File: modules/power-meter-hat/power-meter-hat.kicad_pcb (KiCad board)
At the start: 2 copper layers, 65 x 56 mm, 48 parts, among them J1 GPIO, J2 Barrel_Jack_Switch, J3 Conn_01x02, J4 Conn_01x02, J5 Conn_01x02, U1 CAT24C256, U2 NCP1117-3.3_SOT223, U3 INA219AxD, U4 INA219AxD, U5 INA219AxD

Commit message: Update components and footprints
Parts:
- C1: value 100n -> C_Small
- C2, C3: value 22u -> C
- D1, D2, D3, D4, D5: footprint LED_SMD:LED_1206_3216Metric_Castellated -> LED_SMD:LED_1206_3216Metric
- J1: value GPIO -> Conn_02x20_Odd_Even
- JP1: value ID_WP -> SolderJumper_2_Open
- JP10, JP11, JP3, JP4, JP5, JP6, JP7, JP8, JP9: value Jumper_NC_Dual -> Jumper_3_Open
- JP2: value Jumper -> SolderJumper_2_Open
- R1, R2: value 3.9k -> R_Small
- R10, R12, R3, R4, R8: value 220R -> R
- R11, R7, R9: value ? -> R
- R5, R6: value 10k -> R
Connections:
- net +3V3 renamed +3.3V

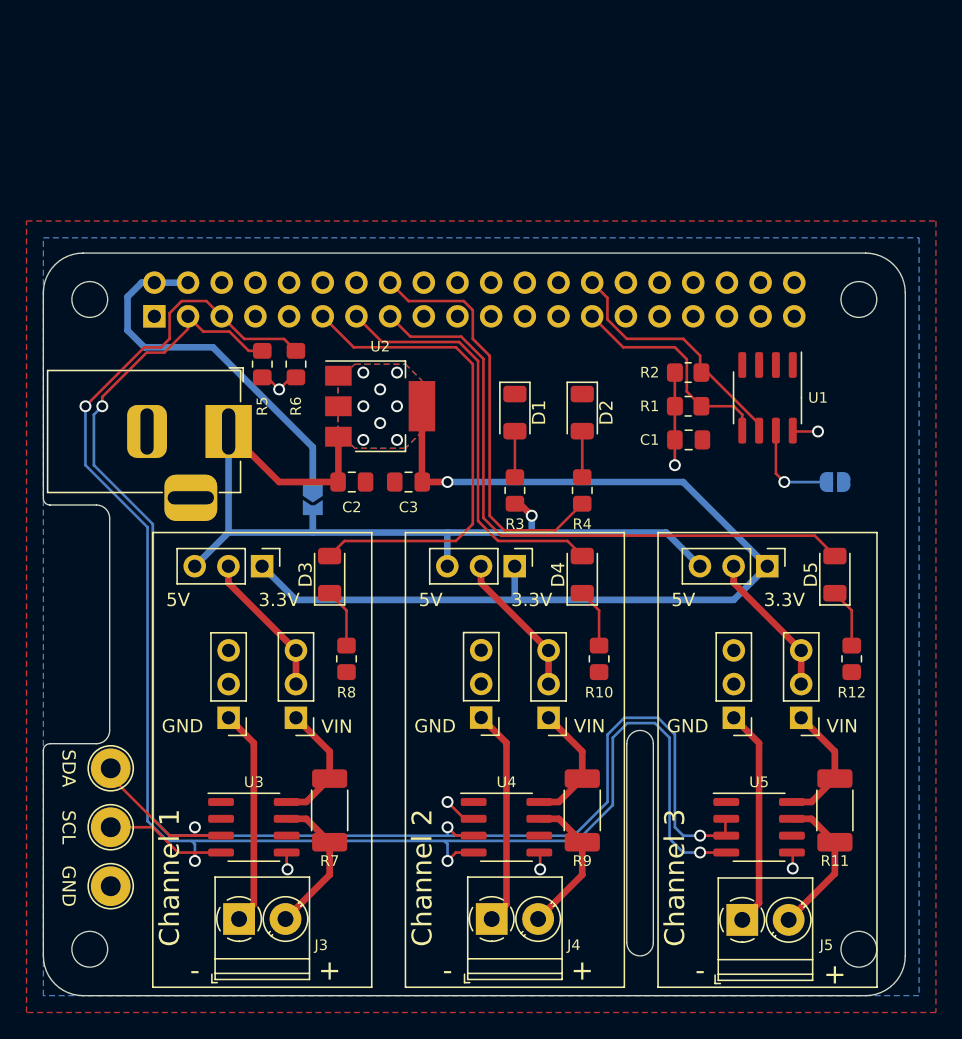
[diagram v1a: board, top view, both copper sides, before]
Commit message: Add "ideal diode" and fuse, update values
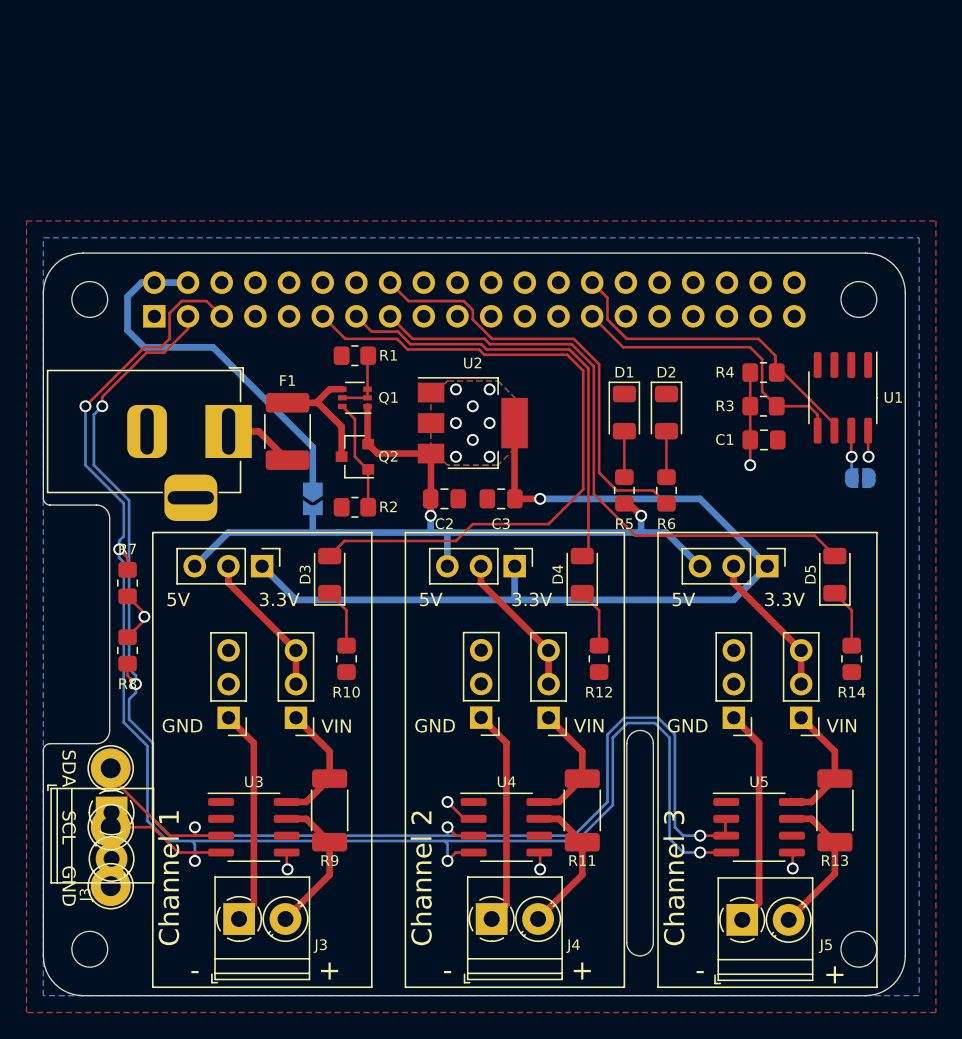
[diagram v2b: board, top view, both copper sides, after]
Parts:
- added F1: MF-MSMF250/16X-2, Fuse:Fuse_1812_4532Metric_Castellated, F.Cu at (118.4, 57.5)
- added J3: OutputTerminal, TerminalBlock_Phoenix:TerminalBlock_Phoenix_PT-1,5-2-3.5-H_1x02_P3.50mm_Horizontal, F.Cu at (105.1, 86.2)
- added Q1: BC856BDW1, Package_TO_SOT_SMD:SOT-363_SC-70-6, F.Cu at (123.5, 54.9)
- added Q2: SI2301CDS, Package_TO_SOT_SMD:SOT-23, F.Cu at (123.5, 59.4)
- added R1: 10k, Resistor_SMD:R_0805_2012Metric_Pad1.20x1.40mm_HandSolder, F.Cu at (123.5, 51.7)
- added R2: 47k, Resistor_SMD:R_0805_2012Metric_Pad1.20x1.40mm_HandSolder, F.Cu at (123.5, 63.2)
- C1: value C_Small -> 100n
- C2, C3: value C -> 22u
- J2: renamed from J1; value Conn_02x20_Odd_Even -> GPIO
- J3, J4, J5: value Conn_01x02 -> OutputTerminal
- JP1: value SolderJumper_2_Open -> ID_WP
- JP10, JP11, JP3, JP4, JP5, JP6, JP7, JP8, JP9: value Jumper_3_Open -> Jumper
- JP2: value SolderJumper_2_Open -> 5V_Bridge
- R10: renamed from R8; value R -> 220R
- R12: renamed from R10; value R -> 220R
- R14: renamed from R12; value R -> 220R
- R3: renamed from R1; value R_Small -> 3.9k
- R4: renamed from R2; value R_Small -> 3.9k
- R5: renamed from R3; value R -> 220R
- R6: renamed from R4; value R -> 220R
- R7: renamed from R5; value R -> 10k
- R8: renamed from R6; value R -> 10k
- moved R7 23.9 mm to (106.3, 74.0), turned to -90 degrees
- moved R8 20.8 mm to (106.3, 68.9)
- moved D1 8.25 mm to (143.8, 56.0)
- moved R5 8.25 mm to (143.8, 61.9)
- moved C3 7.10 mm to (134.5, 62.5)
- moved C2 7.10 mm to (130.2, 62.5)
- moved U2 7.10 mm to (132.4, 56.8)
- moved D2 6.35 mm to (147.0, 56.0)
- moved R6 6.35 mm to (147.0, 61.9)
- moved C1 5.68 mm to (154.3, 58.1)
- moved R3 5.68 mm to (154.3, 55.5)
- moved R4 5.68 mm to (154.3, 53.0)
- moved U1 5.68 mm to (160.3, 54.9)
- moved JP1 1.93 mm to (161.6, 61.0)
- renumbered J2 to J1, R9 to R11, R11 to R13, R7 to R9
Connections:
- J1 pad 1: +5VP -> /Vpsu
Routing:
- net /GPIO[17]: track 36.7 -> 51.5 mm
- net /Vfused: track 0.00 -> 9.44 mm
- net Net-(Q1-Pad6): track 0.00 -> 8.44 mm
- net +3.3VP: track 77.1 -> 69.6 mm
- net +5VP: track 68.4 -> 61.3 mm, vias 1 -> 2
- net /ID_SCL: track 19.2 -> 24.9 mm
- net /ID_SDA: track 17.0 -> 22.7 mm
- net /Vpsu: track 0.00 -> 5.34 mm
- net Net-(Q1-Pad2): track 0.00 -> 5.10 mm
- net /SCL: track 129.7 -> 125.1 mm, vias 4 -> 5
- net /SDA: track 124.5 -> 120.1 mm, vias 4 -> 5
- net Net-(JP1-Pad1): track 7.31 -> 3.59 mm
- net /GPIO[27]: track 31.6 -> 33.5 mm
- net /GPIO[23]: track 31.4 -> 33.0 mm
- net /GPIO[22]: track 48.0 -> 46.7 mm
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
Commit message: Fix PCB
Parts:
- removed the J3 at (105.1, 86.2)
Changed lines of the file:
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@@
-  )
-  (footprint "TerminalBlock_Phoenix:TerminalBlock_Phoenix_PT-1,5-2-3.5-H_1x02_P3.50mm_Horizontal" (layer "F.Cu")
-    (at 105.145 86.185 -90)
-    (descr "Terminal Block Phoenix PT-1,5-2-3.5-H, 2 pins, pitch 3.5mm, size 7x7.6mm^2, drill diamater 1.2mm, pad diameter 2.4mm, see , script-generated using https://github.com/pointhi/kicad-footprint-generator/scripts/TerminalBlock_Phoenix")
-    (tags "THT Terminal Block Phoenix PT-1,5-2-3.5-H pitch 3.5mm size 7x7.6mm^2 drill 1.2mm pad 2.4mm")
-    (property "Sheetfile" "power_channel.kicad_sch")
-    (property "Sheetname" "PowerChannel 1")
-    (attr through_hole)
-    (fp_text reference "J3" (at 6.195 1.97 90) (layer "F.SilkS")
-      (effects (font (size 0.8 0.8) (thickness 0.1)))
-    )
-    (fp_text value "OutputTerminal" (at 1.75 5.56 90) (layer "F.Fab")
-      (effects (font (size 0.6 0.6) (thickness 0.08)))
-    )
-    (fp_text user "${REFERENCE}" (at 1.75 2.605 90) (layer "F.Fab")
-      (effects (font (size 0.8 0.8) (thickness 0.1)))
-    )
-    (fp_line (start 4.57 -1.275) (end 4.476 -1.181) (layer "F.SilkS") (width 0.12))
-    (fp_line (start -1.81 -3.16) (end 5.31 -3.16) (layer "F.SilkS") (width 0.12))
-    (fp_line (start 4.775 -1.069) (end 4.646 -0.941) (layer "F.SilkS") (width 0.12))
-    (fp_line (start 2.525 1.181) (end 2.431 1.274) (layer "F.SilkS") (width 0.12))
-    (fp_line (start 5.31 -3.16) (end 5.31 4.56) (layer "F.SilkS") (width 0.12))
-    (fp_line (start -1.81 4.56) (end 5.31 4.56) (layer "F.SilkS") (width 0.12))
-    (fp_line (start 2.355 0.941) (end 2.226 1.069) (layer "F.SilkS") (width 0.12))
-    (fp_line (start -1.81 -3.16) (end -1.81 4.56) (layer "F.SilkS") (width 0.12))
-    (fp_line (start -1.81 4.1) (end 5.31 4.1) (layer "F.SilkS") (width 0.12))
-    (fp_line (start -1.81 3) (end 5.31 3) (layer "F.SilkS") (width 0.12))
-    (fp_line (start -2.05 4.8) (end -1.65 4.8) (layer "F.SilkS") (width 0.12))
-    (fp_line (start -2.05 4.16) (end -2.05 4.8) (layer "F.SilkS") (width 0.12))
-    (fp_arc (start 0.028674 1.680099) (mid -0.435535 1.622918) (end -0.866 1.44) (layer "F.SilkS") (width 0.12))
-    (fp_arc (start 1.425504 -0.890193) (mid 1.680626 0.000476) (end 1.425 0.891) (layer "F.SilkS") (width 0.12))
-    (fp_arc (start -1.425358 0.889894) (mid -1.680286 0.014012) (end -1.44 -0.866) (layer "F.SilkS") (width 0.12))
-    (fp_arc (start -0.889894 -1.425358) (mid -0.014012 -1.680286) (end 0.866 -1.44) (layer "F.SilkS") (width 0.12))
-    (fp_arc (start 0.890264 1.424721) (mid 0.463071 1.61492) (end 0 1.68) (layer "F.SilkS") (width 0.12))
-    (fp_circle (center 3.5 0) (end 5.18 0) (layer "F.SilkS") (width 0.12) (fill none))
-    (fp_line (start -2.25 5) (end 5.75 5) (layer "F.CrtYd") (width 0.05))
-    (fp_line (start 5.75 5) (end 5.75 -3.6) (layer "F.CrtYd") (width 0.05))
-    (fp_line (start 5.75 -3.6) (end -2.25 -3.6) (layer "F.CrtYd") (width 0.05))
-    (fp_line (start -2.25 -3.6) (end -2.25 5) (layer "F.CrtYd") (width 0.05))
-    (fp_line (start 5.25 -3.1) (end 5.25 4.5) (layer "F.Fab") (width 0.1))
-    (fp_line (start 1.138 -0.955) (end -0.955 1.138) (layer "F.Fab") (width 0.1))
-    (fp_line (start -1.35 4.5) (end -1.75 4.1) (layer "F.Fab") (width 0.1))
-    (fp_line (start -1.75 -3.1) (end 5.25 -3.1) (layer "F.Fab") (width 0.1))
-    (fp_line (start -1.75 3) (end 5.25 3) (layer "F.Fab") (width 0.1))
-    (fp_line (start 4.455 -1.138) (end 2.363 0.955) (layer "F.Fab") (width 0.1))
-    (fp_line (start -1.75 4.1) (end 5.25 4.1) (layer "F.Fab") (width 0.1))
-    (fp_line (start 0.955 -1.138) (end -1.138 0.955) (layer "F.Fab") (width 0.1))
-    (fp_line (start 5.25 4.5) (end -1.35 4.5) (layer "F.Fab") (width 0.1))
-    (fp_line (start 4.638 -0.955) (end 2.546 1.138) (layer "F.Fab") (width 0.1))
-    (fp_line (start -1.75 4.1) (end -1.75 -3.1) (layer "F.Fab") (width 0.1))
-    (fp_circle (center 3.5 0) (end 5 0) (layer "F.Fab") (width 0.1) (fill none))
-    (fp_circle (center 0 0) (end 1.5 0) (layer "F.Fab") (width 0.1) (fill none))
-    (pad "1" thru_hole rect (at 0 0 270) (size 2.4 2.4) (drill 1.2) (layers *.Cu *.Mask)
-      (net 32 "/PowerChannel 1/OUT_GND") (pinfunction "Pin_1") (pintype "passive"))
-    (pad "2" thru_hole circle (at 3.5 0 270) (size 2.4 2.4) (drill 1.2) (layers *.Cu *.Mask)
-      (net 31 "/PowerChannel 1/OUT_VCC") (pinfunction "Pin_2") (pintype "passive"))
-    (model "${KICAD6_3DMODEL_DIR}/TerminalBlock_Phoenix.3dshapes/TerminalBlock_Phoenix_PT-1,5-2-3.5-H_1x02_P3.50mm_Horizontal.wrl"
-      (offset (xyz 0 0 0))
-      (scale (xyz 1 1 1))
-      (rotate (xyz 0 0 0))
-    )
   )
   (footprint "TerminalBlock_Phoenix:TerminalBlock_Phoenix_PT-1,5-2-3.5-H_1x02_P3.50mm_Horizontal" (layer "F.Cu")

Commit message: Change jumpers
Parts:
- removed J4: OutputTerminal, TerminalBlock_Phoenix:TerminalBlock_Phoenix_PT-1,5-2-3.5-H_1x02_P3.50mm_Horizontal
- removed JP10: Jumper, Connector_PinHeader_2.54mm:PinHeader_1x03_P2.54mm_Vertical
- removed the JP4 at (114.0, 79.0)
- removed the JP7 at (133.0, 79.0)
- added J7: OutputTerminal, TerminalBlock_Phoenix:TerminalBlock_Phoenix_PT-1,5-4-3.5-H_1x04_P3.50mm_Horizontal, F.Cu at (149.4, 87.9)
- F1: footprint Fuse:Fuse_1812_4532Metric_Castellated -> Fuse:Fuse_1812_4532Metric
- J3, J5: footprint TerminalBlock_Phoenix:TerminalBlock_Phoenix_PT-1,5-2-3.5-H_1x02_P3.50mm_Horizontal -> TerminalBlock_Phoenix:TerminalBlock_Phoenix_PT-1,5-4-3.5-H_1x04_P3.50mm_Horizontal
- moved J5 23.3 mm to (130.3, 87.9)
- moved R14 13.6 mm to (150.2, 66.3), turned to -90 degrees
- moved R10 13.6 mm to (112.1, 66.3), turned to -90 degrees
- moved R12 13.6 mm to (131.1, 66.3), turned to -90 degrees
- moved D3 12.2 mm to (109.5, 66.3)
- moved D4 12.2 mm to (128.6, 66.3)
- moved D5 12.2 mm to (147.6, 66.3)
- moved JP7 7.40 mm to (153.4, 72.7), turned to 90 degrees
- moved JP3 7.40 mm to (115.3, 72.7), turned to 90 degrees
- moved JP5 7.40 mm to (134.3, 72.7), turned to 90 degrees
- moved J3 7.25 mm to (111.3, 87.9)
- moved U4 7.01 mm to (134.3, 80.3)
- moved U3 7.01 mm to (115.2, 80.3)
- moved U5 7.01 mm to (153.3, 80.3)
- moved R11 6.98 mm to (140.6, 79.0)
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- renumbered JP5 to JP4, JP6 to JP5, JP8 to JP6, JP9 to JP7, JP11 to JP8
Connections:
- J3 pad 1: /PowerChannel 1/OUT_GND -> /PowerChannel 1/EXTERNAL_VIN
- J3 pad 2: /PowerChannel 1/OUT_VCC -> GND
- J5 pad 1: /PowerChannel 3/OUT_GND -> /PowerChannel 2/EXTERNAL_VIN
- J5 pad 2: /PowerChannel 3/OUT_VCC -> GND
- JP3 pad 1: /PowerChannel 1/IN_VCC -> /PowerChannel 1/EXTERNAL_VIN
- JP3 pad 2: /PowerChannel 1/PWR -> /PowerChannel 1/VIN
- JP3 pad 3: /PowerChannel 1/PWR -> /PowerChannel 1/INTERNAL_VIN
- JP4 pad 2: /PowerChannel 1/PWR -> /PowerChannel 1/INTERNAL_VIN
- JP5 pad 1: /PowerChannel 2/IN_VCC -> /PowerChannel 2/EXTERNAL_VIN
- JP5 pad 2: /PowerChannel 2/PWR -> /PowerChannel 2/VIN
- JP5 pad 3: /PowerChannel 2/PWR -> /PowerChannel 2/INTERNAL_VIN
- JP6 pad 2: /PowerChannel 2/PWR -> /PowerChannel 2/INTERNAL_VIN
- JP7 pad 1: /PowerChannel 3/IN_VCC -> /PowerChannel 3/EXTERNAL_VIN
- JP7 pad 2: /PowerChannel 3/PWR -> /PowerChannel 3/VIN
- JP7 pad 3: /PowerChannel 3/PWR -> /PowerChannel 3/INTERNAL_VIN
- JP8 pad 2: /PowerChannel 3/PWR -> /PowerChannel 3/INTERNAL_VIN
- R11 pad 1: /PowerChannel 2/IN_VCC -> /PowerChannel 2/VIN
- R11 pad 2: /PowerChannel 2/OUT_VCC -> /PowerChannel 2/VOUT
- R13 pad 1: /PowerChannel 3/IN_VCC -> /PowerChannel 3/VIN
- R13 pad 2: /PowerChannel 3/OUT_VCC -> /PowerChannel 3/VOUT
- R9 pad 1: /PowerChannel 1/IN_VCC -> /PowerChannel 1/VIN
- R9 pad 2: /PowerChannel 1/OUT_VCC -> /PowerChannel 1/VOUT
- U3 pad 7: /PowerChannel 1/OUT_VCC -> /PowerChannel 1/VOUT
- U3 pad 8: /PowerChannel 1/IN_VCC -> /PowerChannel 1/VIN
- U4 pad 7: /PowerChannel 2/OUT_VCC -> /PowerChannel 2/VOUT
- U4 pad 8: /PowerChannel 2/IN_VCC -> /PowerChannel 2/VIN
- U5 pad 7: /PowerChannel 3/OUT_VCC -> /PowerChannel 3/VOUT
- U5 pad 8: /PowerChannel 3/IN_VCC -> /PowerChannel 3/VIN
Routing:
- net /SDA: track 120.1 -> 96.2 mm, vias 5 -> 6
- net /SCL: track 125.1 -> 103.4 mm, vias 5 -> 6
- net /PowerChannel 2/EXTERNAL_VIN: track 0.00 -> 21.0 mm
- net /PowerChannel 1/EXTERNAL_VIN: track 0.00 -> 21.0 mm
- net /PowerChannel 3/EXTERNAL_VIN: track 0.00 -> 21.0 mm
- net /PowerChannel 3/OUT_GND: track 16.6 -> 0.00 mm
- net /PowerChannel 2/OUT_GND: track 16.4 -> 0.00 mm
- net /PowerChannel 1/OUT_GND: track 16.4 -> 0.00 mm
- net /GPIO[22]: track 46.7 -> 33.6 mm
- net /PowerChannel 1/VOUT: track 0.00 -> 12.4 mm
- net /PowerChannel 3/VOUT: track 0.00 -> 12.4 mm
- net /PowerChannel 2/VOUT: track 0.00 -> 12.4 mm
- net /PowerChannel 3/OUT_VCC: track 11.3 -> 0.00 mm
- net /PowerChannel 1/OUT_VCC: track 11.1 -> 0.00 mm
- net /PowerChannel 2/OUT_VCC: track 11.1 -> 0.00 mm
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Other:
- board text added: "GND"
- board text added: "VIN"
- board text added: "VOUT"
- board text removed: "+"
- board text removed: "-"

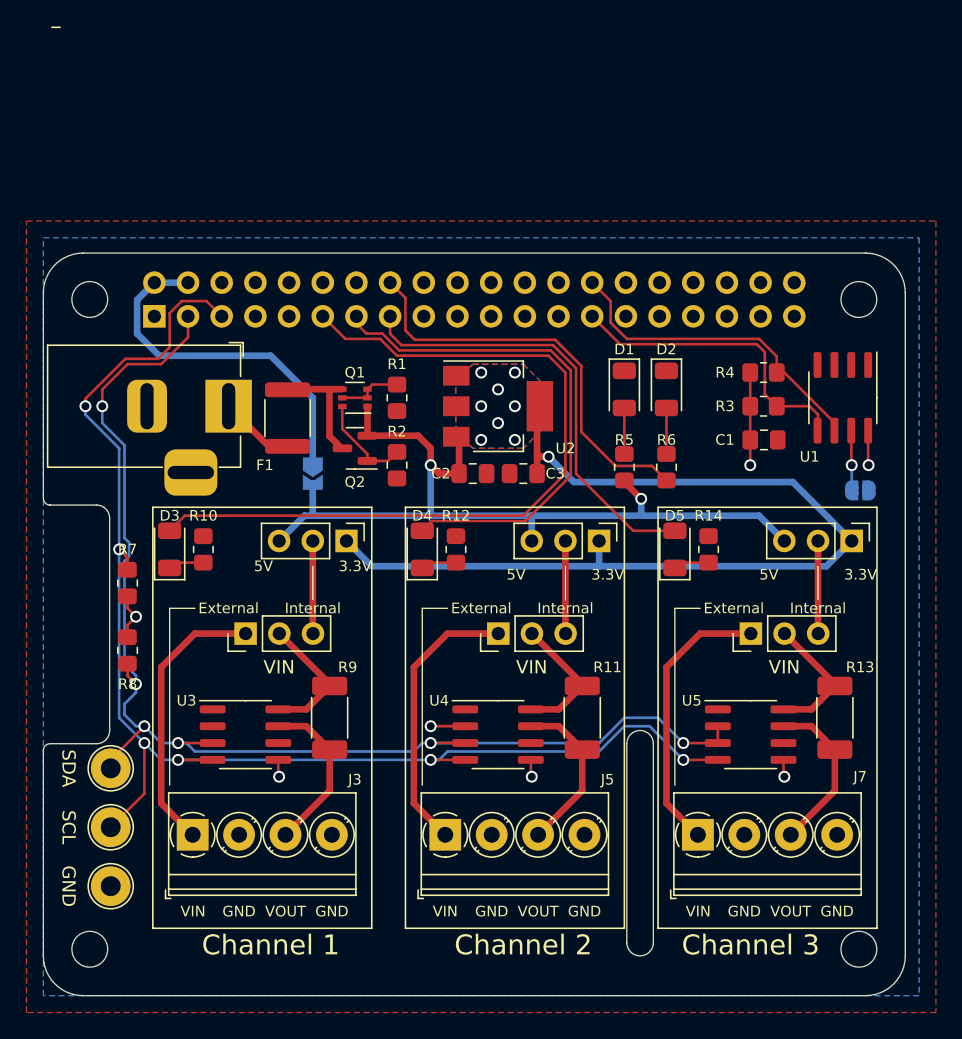
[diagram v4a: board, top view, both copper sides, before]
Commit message: Switch power and ground plane (power top. ground bottom)
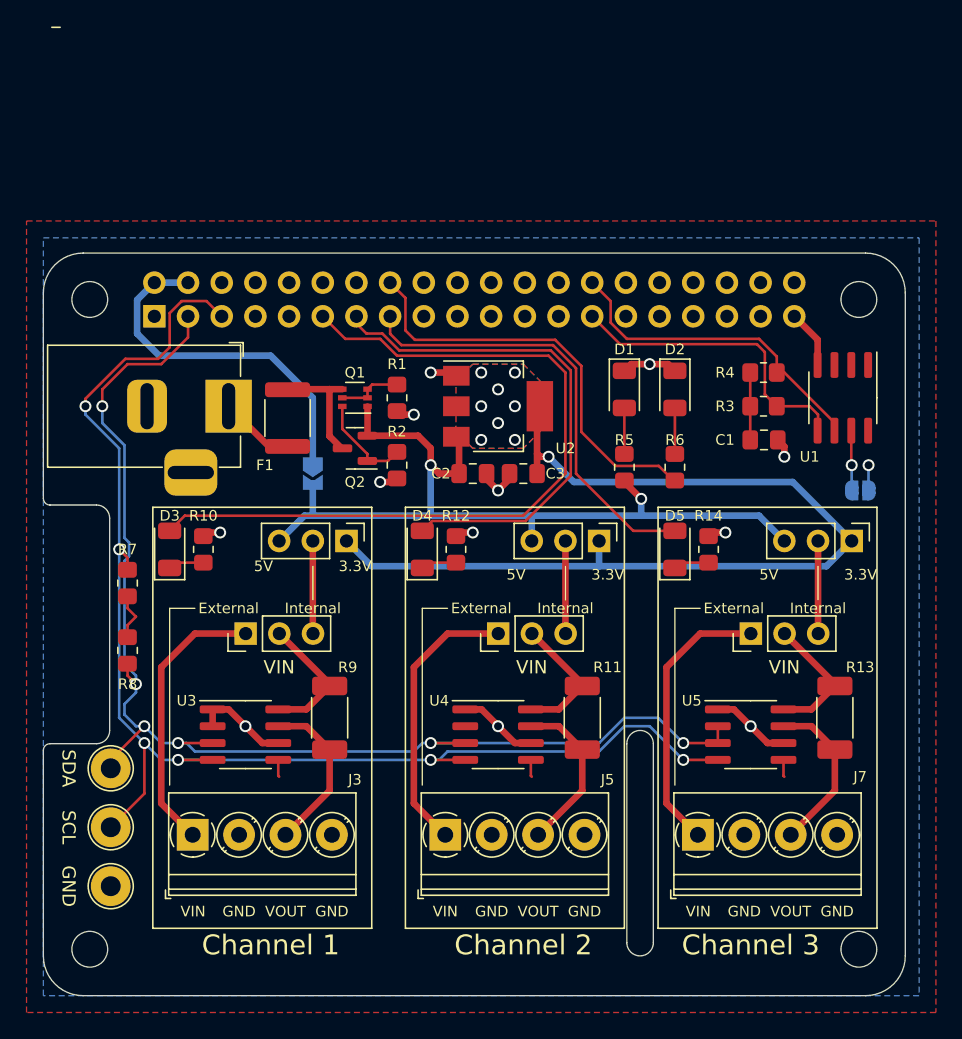
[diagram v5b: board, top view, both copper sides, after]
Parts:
- moved D2 0.63 mm to (147.6, 54.3)
- moved R6 0.63 mm to (147.6, 60.1)
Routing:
- net GND: track 0.00 -> 41.6 mm, vias 0 -> 12
- net +3.3V: track 19.7 -> 14.5 mm, vias 7 -> 1
- net /GPIO[23]: track 31.4 -> 31.9 mm
- added copper zone on F.Cu, net +3.3V
- added copper zone on B.Cu, net GND
- removed copper zone on B.Cu, net +3.3V
- removed copper zone on F.Cu, net GND

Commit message: Cleanup schematic & PCB
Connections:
- net /GPIO[17] renamed /LED_CH1
- net /GPIO[22] renamed /LED_CH3
- net /GPIO[23] renamed /LED
- net /GPIO[27] renamed /LED_CH2
- J2 pad 10: /GPIO[15]/RXD0 -> unconnected-(J2-Pad10)
- J2 pad 12: /GPIO[18]/PCM.CLK -> unconnected-(J2-Pad12)
- J2 pad 18: /GPIO[24] -> unconnected-(J2-Pad18)
- J2 pad 19: /GPIO[10]/SPI0.MOSI -> unconnected-(J2-Pad19)
- J2 pad 21: /GPIO[9]/SPI0.MISO -> unconnected-(J2-Pad21)
- J2 pad 22: /GPIO[25] -> unconnected-(J2-Pad22)
- J2 pad 23: /GPIO[11]/SPI0.SCLK -> unconnected-(J2-Pad23)
- J2 pad 24: /GPIO[8]/SPI0.CE0 -> unconnected-(J2-Pad24)
- J2 pad 26: /GPIO[7]/SPI0.CE1 -> unconnected-(J2-Pad26)
- J2 pad 29: /GPIO[5] -> unconnected-(J2-Pad29)
- J2 pad 31: /GPIO[6] -> unconnected-(J2-Pad31)
- J2 pad 32: /GPIO[12]/PWM0 -> unconnected-(J2-Pad32)
- J2 pad 33: /GPIO[13]/PWM1 -> unconnected-(J2-Pad33)
- J2 pad 35: /GPIO[19]/PCM.FS -> unconnected-(J2-Pad35)
- J2 pad 36: /GPIO[16] -> unconnected-(J2-Pad36)
- J2 pad 37: /GPIO[26] -> unconnected-(J2-Pad37)
- J2 pad 38: /GPIO[20]/PCM.DIN -> unconnected-(J2-Pad38)
- J2 pad 40: /GPIO[21]/PCM.DOUT -> unconnected-(J2-Pad40)
- J2 pad 7: /GPIO[4]/GPCLK0 -> unconnected-(J2-Pad7)
- J2 pad 8: /GPIO[14]/TXD0 -> unconnected-(J2-Pad8)
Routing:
- net GND: track 41.6 -> 32.7 mm, vias 12 -> 15
- net +3.3V: track 14.5 -> 10.6 mm
- net +5VP: track 64.9 -> 63.3 mm
- net /Vpsu: track 5.71 -> 4.32 mm
- net /SDA: track 96.2 -> 95.5 mm
- net /ID_SCL: track 24.9 -> 24.3 mm
- net Net-(D5-Pad1): track 2.71 -> 2.14 mm
- net Net-(D4-Pad1): track 2.71 -> 2.14 mm
- net Net-(D3-Pad1): track 2.71 -> 2.14 mm
- net /LED_CH2: track 39.0 -> 38.5 mm
